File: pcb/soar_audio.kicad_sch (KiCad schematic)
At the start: 34 parts

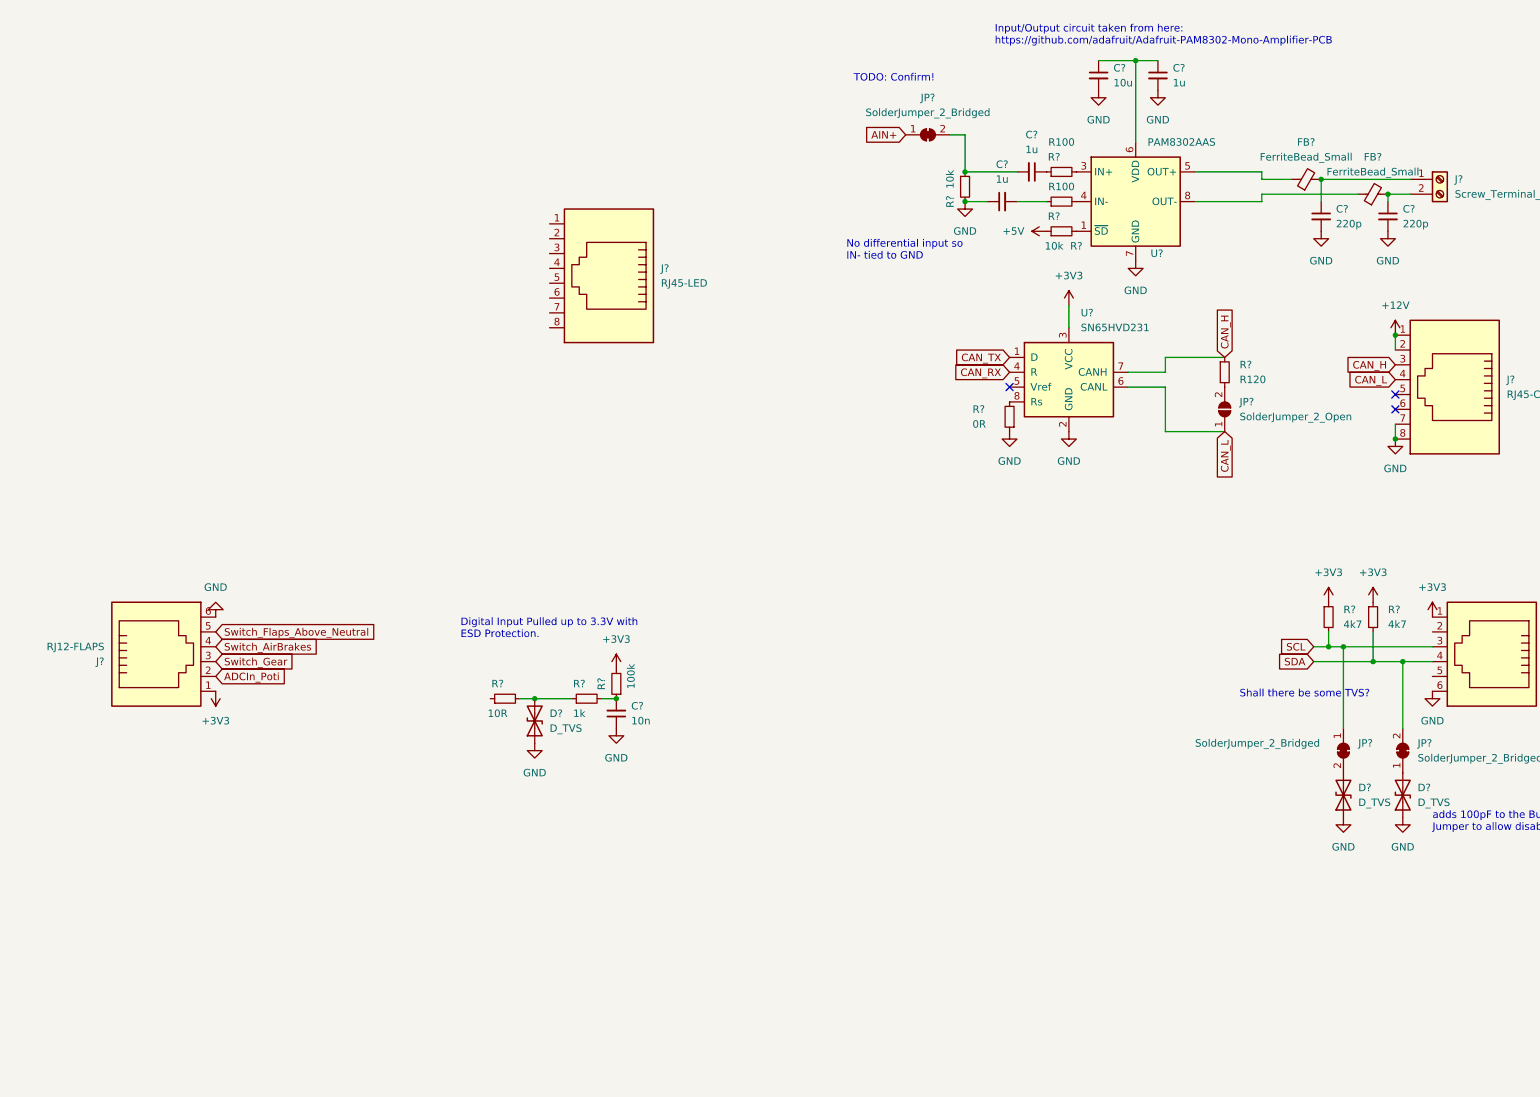
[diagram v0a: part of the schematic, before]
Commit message: added dcdc power supply
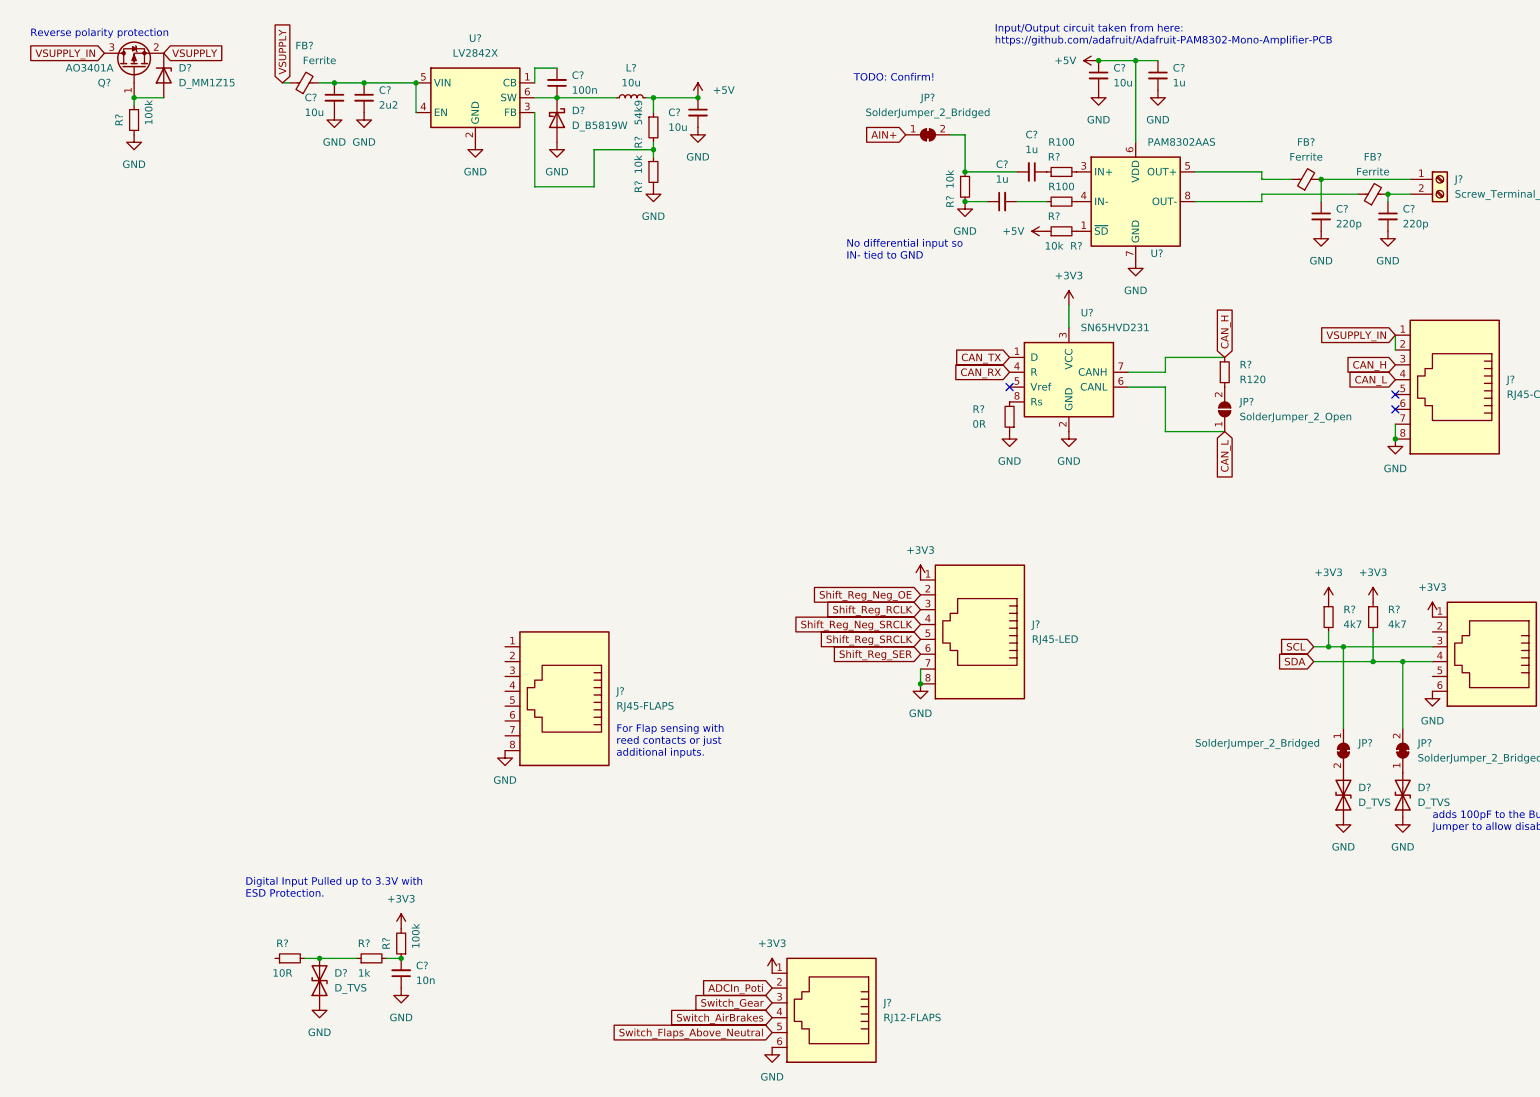
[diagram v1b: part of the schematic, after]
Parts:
- added C? (x2): 10u, Capacitor_SMD:C_0805_2012Metric, symbol Device:C_Small
- added C?: 100n, Capacitor_SMD:C_0603_1608Metric, symbol Device:C_Small
- added C?: 2u2, Capacitor_SMD:C_0805_2012Metric, symbol Device:C_Small
- added D?: D_B5819W, Diode_SMD:D_SOD-123, symbol Device:D_Schottky
- added D?: D_MM1Z15, Diode_SMD:D_SOD-123, symbol Device:D_Zener
- added FB?: Ferrite, Inductor_SMD:L_0805_2012Metric, symbol Device:FerriteBead_Small
- added J?: RJ45-FLAPS, RJ45_Amphenol_RJHSE5380, symbol Connector:RJ45
- added L?: 10u, Inductor_SMD:L_Bourns-SRN4018, symbol Device:L_Small
- added Q?: AO3401A, Package_TO_SOT_SMD:SOT-23, symbol Transistor_FET:AO3401A
- added R?: 100k, Resistor_SMD:R_0603_1608Metric, symbol Device:R_Small
- added R?: 10k, Resistor_SMD:R_0603_1608Metric, symbol Device:R_Small
- added R?: 54k9, Resistor_SMD:R_0603_1608Metric, symbol Device:R_Small
- added U?: LV2842X, Package_TO_SOT_SMD:TSOT-23-6, symbol lv2842x:LV2842X
- FB? (x2): value FerriteBead_Small -> Ferrite
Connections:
- net +3V3: now also J?.1
- net +5V: now also C?.1, C?.1, U?.6 (VDD), C?.1, L?.2, R?.1
- net GND: now also J?.7, J?.8, C?.2, C?.2, C?.2, D?.2 (A), J?.8, R?.1, R?.2, U?.2 (GND)
- net Shift_Reg_Neg_OE: now reaches J?.2
- net Shift_Reg_RCLK: now reaches J?.3
- net Shift_Reg_Neg_SRCLK: now reaches J?.4
- net Shift_Reg_SRCLK: now reaches J?.5
- net Shift_Reg_SER: now reaches J?.6
- net +12V renamed VSUPPLY_IN
- net VSUPPLY_IN: now also Q?.3 (D)
- new net: C?.2, U?.1 (CB)
- new net: R?.1, R?.2, U?.3 (FB)
- new net: C?.1, C?.1, FB?.2, U?.4 (EN), U?.5 (VIN)
- new net: C?.1, D?.1 (K), L?.1, U?.6 (SW)
- new net: D?.2 (A), Q?.1 (G), R?.2
- new net VSUPPLY: D?.1 (K), FB?.1, Q?.2 (S)
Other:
- note added: "For Flap sensing with reed contacts or just additional inputs."
- note added: "Reverse polarity protection"
- note removed: "Shall there be some TVS?"
- moved on the sheet: C?, D?, J?, R?

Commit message: added 3v3 power supply
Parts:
- added C?: 100n, Capacitor_SMD:C_0603_1608Metric, symbol Device:C_Small
- added C?: 2u2, Capacitor_SMD:C_0805_2012Metric, symbol Device:C_Small
- added C? (x3): 10u, Capacitor_SMD:C_0805_2012Metric, symbol Device:C_Small
- added D?: D_B5819W, Diode_SMD:D_SOD-123, symbol Device:D_Schottky
- added FB?: Ferrite, Inductor_SMD:L_0805_2012Metric, symbol Device:FerriteBead_Small
- added L?: 10u, Inductor_SMD:L_Bourns-SRN4018, symbol Device:L_Small
- added R?: 33k2, Resistor_SMD:R_0603_1608Metric, symbol Device:R_Small
- added R?: 10k, Resistor_SMD:R_0603_1608Metric, symbol Device:R_Small
- added U?: LV2842X, Package_TO_SOT_SMD:TSOT-23-6, symbol lv2842x:LV2842X
- JP? (x3): value SolderJumper_2_Bridged -> Jumper_Bridged
- JP?: value SolderJumper_2_Open -> Jumper_Open
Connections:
- net +3V3: now also C?.1, L?.2, R?.1
- net GND: now also C?.2, C?.2, C?.2, C?.2, D?.2 (A), R?.2, U?.2 (GND)
- net VSUPPLY: now also C?.1, FB?.1
- new net: C?.2, U?.1 (CB)
- new net: R?.1, R?.2, U?.3 (FB)
- new net: C?.1, C?.1, FB?.2, U?.4 (EN), U?.5 (VIN)
- new net: C?.1, D?.1 (K), L?.1, U?.6 (SW)
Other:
- moved on the sheet: C?, D?, FB?, L?, Q?, R?, U?

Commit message: updated with bluepill and discovery board footprint
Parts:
- added C17, C18, C19, C20, C21, C22, C23, C24, C25, C26: 10n, Capacitor_SMD:C_0603_1608Metric, symbol Device:C_Small
- added D10, D11, D12, D13, D14, D15, D16, D17, D18, D19, D20, D21, D7, D8, D9: D_TVS, Diode_SMD:D_SOD-323, symbol Device:D_TVS
- added J7: STM32F4_Discovery_Header, STM32F4Di:stm32f4_discovery_header, symbol STM32F4Di:STM32F4_Discovery_Header
- added R17, R20, R21, R26, R29, R32, R35, R38, R41, R44: 1k, Resistor_SMD:R_0805_2012Metric, symbol Device:R_Small
- added R18, R22, R23, R27, R30, R33, R36, R39, R42, R45: 1k, Resistor_SMD:R_0603_1608Metric, symbol Device:R_Small
- added R19, R24, R25, R28, R31, R34, R37, R40, R43: 100k, Resistor_SMD:R_0603_1608Metric, symbol Device:R_Small
- added U5: HAMMOND_1593W, OWN_PARTS:HAMMOND_1593W_edge_cut_notallmountingholes, symbol OWN_PARTS:HAMMOND_1593W
- added U6: BP, Bluepill:blue_pill, symbol Bluepill:BP
- Q1: renamed from Q?; LCSC (none) -> C15127
- R2: renamed from R?; value 10R -> 1k; footprint Resistor_SMD:R_0603_1608Metric -> Resistor_SMD:R_0805_2012Metric; LCSC C22859 -> C17513
- gave numbers to parts that had none: 57
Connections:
- net +3V3: now also R19.2, R24.2, R25.2, R28.2, R31.2, R34.2, R37.2, R40.2, R43.2
- net GND: now also C17.1, C18.1, C19.1, C20.1, C21.1, C22.1, C23.1, C24.1, C25.1, C26.1, D10.1 (A1), D11.1 (A1), D12.1 (A1), D13.1 (A1), D14.1 (A1), D15.1 (A1), D16.1 (A1), D17.1 (A1), D18.1 (A1), D19.1 (A1), D20.1 (A1), D21.1 (A1), D7.1 (A1), D8.1 (A1), D9.1 (A1)
- net Shift_Reg_Neg_OE: now also D11.2 (A2)
- net Shift_Reg_Neg_SRCLK: now also D9.2 (A2)
- net Shift_Reg_RCLK: now also D10.2 (A2)
- net Shift_Reg_SER: now also D7.2 (A2)
- net Shift_Reg_SRCLK: now also D8.2 (A2)
- net Flaps_Input1: now reaches J1.1
- net Flaps_Input1: now also R2.1
- net Flaps_Input2: now reaches J1.2
- net Flaps_Input2: now also R20.1
- net Flaps_Input3: now reaches J1.3
- net Flaps_Input3: now also R17.1
- net Flaps_Input4: now reaches J1.4
- net Flaps_Input4: now also R21.1
- net Flaps_Input5: now reaches J1.5
- net Flaps_Input5: now also R26.1
- net Flaps_Input6: now reaches J1.6
- net Flaps_Input6: now also R29.1
- net Flaps_Input7: now reaches J1.7
- net Flaps_Input7: now also R32.1
- net Flaps_In1: now reaches C6.2, R3.2, R4.1
- net ADCIn_Poti renamed ADCInput
- net ADCInput: now also R44.1
- net Switch_AirBrakes renamed Switch_AirBrakes_Input
- net Switch_AirBrakes_Input: now also R38.1
- net Switch_Flaps_Above_Neutral renamed Switch_Flaps_Above_Neutral_Input
- net Switch_Flaps_Above_Neutral_Input: now also R41.1
- net Switch_Gear renamed Switch_Gear_Input
- net Switch_Gear_Input: now also R35.1
- new net: D17.2 (A2), R32.2, R33.1
- new net: D21.2 (A2), R44.2, R45.1
- new net: D16.2 (A2), R29.2, R30.1
- new net: D14.2 (A2), R21.2, R23.1
- new net: D18.2 (A2), R35.2, R36.1
- new net: D19.2 (A2), R38.2, R39.1
- new net: D20.2 (A2), R41.2, R42.1
- new net: D12.2 (A2), R17.2, R18.1
- new net: D13.2 (A2), R20.2, R22.1
- new net: D15.2 (A2), R26.2, R27.1
- new net ADCIn: C26.2, R45.2
- new net Flaps_In2: C18.2, R22.2, R24.1
- new net Flaps_In3: C17.2, R18.2, R19.1
- new net Flaps_In4: C19.2, R23.2, R25.1
- new net Flaps_In5: C20.2, R27.2, R28.1
- new net Flaps_In6: C21.2, R30.2, R31.1
- new net Flaps_In8: C22.2, R33.2, R34.1
- new net Switch_AirBrakes_In: C24.2, R39.2, R40.1
- new net Switch_Flaps_Above_Neutral_In: C25.2, R42.2, R43.1
- new net Switch_Gear_In: C23.2, R36.2, R37.1
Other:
- note added: "Digital Input Pulled up to 3.3V with ESD Protection.Save to apply 12V."
- note removed: "Digital Input Pulled up to 3.3V with ESD Protection."
- moved on the sheet: C10, C11, C12, C13, C14, C15, C16, C2, C3, C4, C5, C6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

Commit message: updated schematic and layout
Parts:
- removed C10: 10u, Capacitor_SMD:C_0805_2012Metric, symbol Device:C_Small
- removed C23, C24, C25: 10n, Capacitor_SMD:C_0603_1608Metric, symbol Device:C_Small
- removed C8: 100n, Capacitor_SMD:C_0603_1608Metric, symbol Device:C_Small
- removed D10, D11, D18, D19, D20, D7, D8, D9: D_TVS, Diode_SMD:D_SOD-323, symbol Device:D_TVS
- removed D4: D_B5819W, Diode_SMD:D_SOD-123, symbol Device:D_Schottky
- removed FB2: Ferrite, Inductor_SMD:L_0805_2012Metric, symbol Device:FerriteBead_Small
- removed J3: RJ45-LED, RJ45_Amphenol_RJHSE5380, symbol Connector:RJ45
- removed J6: RJ12-I2C, Connector_RJ:RJ12_Amphenol_54601, symbol Connector:RJ12
- removed J7: STM32F4_Discovery_Header, STM32F4Di:stm32f4_discovery_header, symbol STM32F4Di:STM32F4_Discovery_Header
- removed L2: 10u, Inductor_SMD:L_Bourns-SRN4018, symbol Device:L_Small
- removed U2: LV2842X, Package_TO_SOT_SMD:TSOT-23-6, symbol lv2842x:LV2842X
- removed U5: HAMMOND_1593W, OWN_PARTS:HAMMOND_1593W_edge_cut_notallmountingholes, symbol OWN_PARTS:HAMMOND_1593W
- added D4: D_TVS, Diode_SMD:D_SOD-323, symbol Device:D_TVS
- added J3, J6: HEADER_4, Connector_PinHeader_1.27mm:PinHeader_1x04_P1.27mm_Vertical, symbol STM32F4Di:HEADER_4
- added JP5: Jumper_Open, Jumper:SolderJumper-2_P1.3mm_Open_Pad1.0x1.5mm, symbol Jumper:SolderJumper_2_Open
- added R46: 4k7, Resistor_SMD:R_0603_1608Metric, symbol Device:R_Small
- added R47: 10k, Resistor_SMD:R_0603_1608Metric, symbol Device:R_Small
- C3: value 10u -> 100n; footprint Capacitor_SMD:C_0805_2012Metric -> Capacitor_SMD:C_0603_1608Metric; LCSC C440198 -> C14663
- C5: value 2u2 -> 10n; footprint Capacitor_SMD:C_0805_2012Metric -> Capacitor_SMD:C_0603_1608Metric; LCSC C49217 -> C57112
- R35: value 1k -> 120k; footprint Resistor_SMD:R_0805_2012Metric -> Resistor_SMD:R_0603_1608Metric; LCSC C17513 -> C25808
- R36: value 1k -> 120k; LCSC C21190 -> C25808
- R37: value 100k -> 56k; LCSC C25803 -> C23206
- R38: value 1k -> 30k; footprint Resistor_SMD:R_0805_2012Metric -> Resistor_SMD:R_0603_1608Metric; LCSC C17513 -> C22984
- R39: value 1k -> 15k; LCSC C21190 -> C22809
- R40: value 100k -> 7k5; LCSC C25803 -> C23234
- R41: value 1k -> 3k6; footprint Resistor_SMD:R_0805_2012Metric -> Resistor_SMD:R_0603_1608Metric; LCSC C17513 -> C22980
- R42: value 1k -> 1k8; LCSC C21190 -> C4177
- R43: value 100k -> 4k7; LCSC C25803 -> C23162
- R7: value 33k2 -> 1k; footprint Resistor_SMD:R_0603_1608Metric -> Resistor_SMD:R_0805_2012Metric; LCSC C23003 -> C17513
- R8: value 10k -> 1k; LCSC C25804 -> C21190
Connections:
- net ADCIn is gone; now on net ADC_In1: C26.2, R45.2
- net Flaps_In8 is gone; now on net Flaps_In7: C22.2, R33.2, R34.1
- net Switch_Gear_In is gone; now on net AIN+: R36.2, R37.1
- net +3V3: now also R43.1, U6.3V3 (3.3V), J3.2, J6.2, R46.1; no longer R37.2, R40.2, R43.2, R7.1
- net +5V: now also U6.5V
- net AIN+: now also R35.1, R38.1, R39.1, R40.1, R41.1, R42.1
- net CAN_RX: now also U6.PB8
- net CAN_TX: now also U6.PB9
- net Flaps_In1: now also U6.PB12
- net Flaps_In2: now also U6.PB13
- net Flaps_In3: now also U6.PB14
- net Flaps_In4: now also U6.PB15
- net Flaps_In5: now also U6.PA8
- net Flaps_In6: now also U6.PA9
- net Flaps_Input6: now also J2.4
- net Flaps_Input7: now also J2.5
- net GND: now also C3.1, C5.1, U6.G (GND), D4.1 (A1), J3.1, J6.1, R47.2; no longer C3.2, C5.2, R8.2
- net SCL: now also U6.PB6, J6.3
- net SDA: now also U6.PB7, J6.4
- net PWM_A: now reaches U6.PA0
- net PWM_A: now also R35.2
- net PWM_B: now reaches U6.PA1
- net PWM_B: now also R36.1
- net Flaps_In7: now reaches U6.PA10
- net ATTN_1: now reaches U6.PA2
- net ATTN_1: now also R37.2
- net ATTN_2: now reaches U6.PA3
- net ATTN_2: now also R38.2
- net ATTN_3: now reaches U6.PA4
- net ATTN_3: now also R39.2
- net ATTN_4: now reaches U6.PA5
- net ATTN_4: now also R40.2
- net ATTN_5: now reaches U6.PA6
- net ATTN_5: now also R41.2
- net ATTN_6: now reaches U6.PA7
- net ATTN_6: now also R42.2
- net ADC_In1: now reaches U6.PB0
- net ADC_In2: now reaches U6.PB1
- net ADC_In2: now also C5.2, R8.2
- net SCL2: now reaches U6.PB10
- net SCL2: now also R43.2, J3.3
- net SDA2: now reaches U6.PB11
- net SDA2: now also J3.4, R46.2
- net at R7.2, R8.1: now also D4.2 (A2)
- net at C12.2, JP1.2 (B), R9.1: now also JP5.1 (A)
- net at C2.1, C4.1, FB1.2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: now also C3.2
- net ADCInput renamed ADC_Input1
- removed net Switch_AirBrakes_In: R39.2, R40.1
- removed net Switch_AirBrakes_Input: J2.4, R38.1
- removed net Switch_Flaps_Above_Neutral_In: R42.2, R43.1
- removed net Switch_Flaps_Above_Neutral_Input: J2.5, R41.1
- net Switch_Gear_Input renamed ADC_Input2
- net ADC_Input2: now also R7.1; no longer R35.1
- new net: JP5.2 (B), R47.1
- no-connect marks 3 -> 15
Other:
- note added: "32kHz Crystal"
- note added: "3V3 + GND + 5 Ausgänge 16LEDs"
- note added: "Jumper Header"
- note added: "LED"
- note added: "MOSI1 MISO1 SCK1 NSS1"
- note added: "Micro USB"
- note removed: "TODO: Confirm!"
- moved on the sheet: C26, D21, J1, J2, J5, JP2, R10, R14, R44, R45, U3, U6
